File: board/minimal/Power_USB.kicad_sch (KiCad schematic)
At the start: 11 parts, among them J2 USB_C_Receptacle_USB2.0_16P, U4 STUSB4500QTR

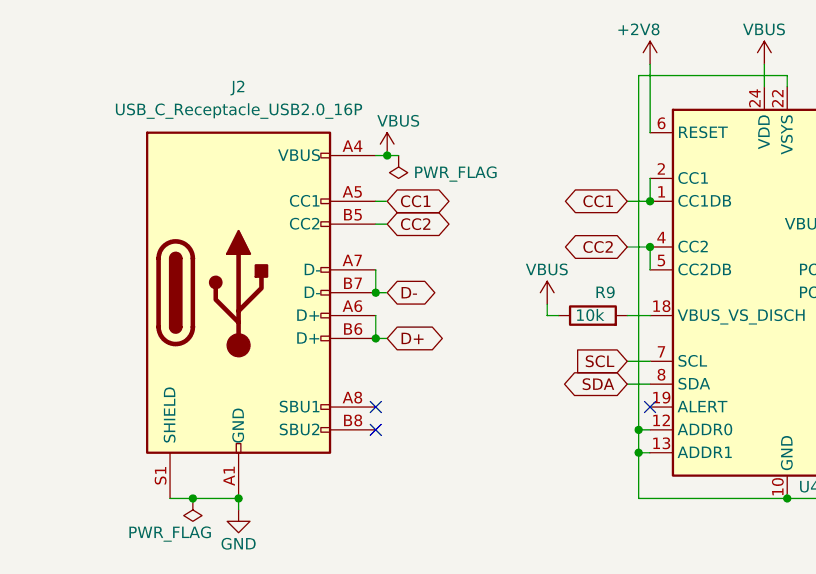
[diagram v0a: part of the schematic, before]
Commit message: change core to rp2350b and some pin out
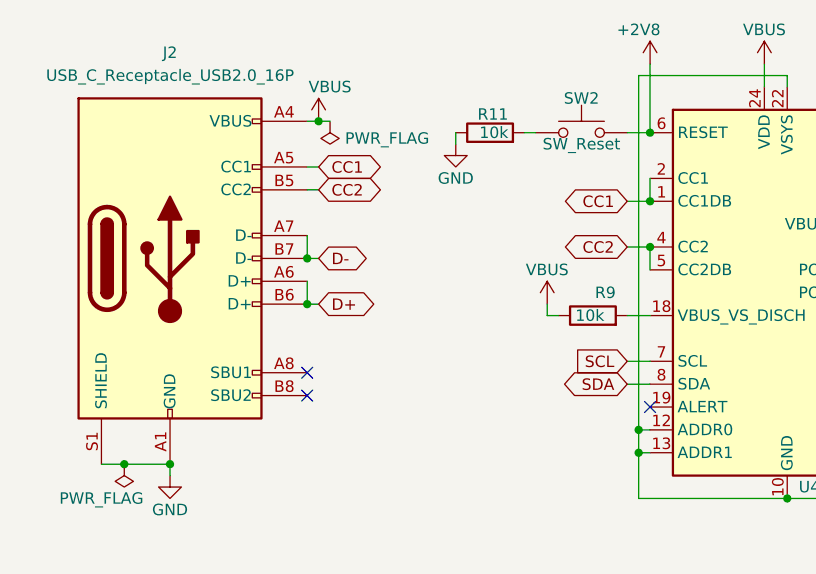
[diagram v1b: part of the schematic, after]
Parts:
- added R11: 10k, Resistor_SMD:R_0603_1608Metric, symbol Device:R
- added SW2: SW_Reset, SW_SKRPACE010:SW_SKRPACE010, symbol Switch:SW_Push
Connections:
- net +2V8: now also SW2.2
- net GND: now also R11.1
- new net: R11.2, SW2.1
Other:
- moved on the sheet: J2

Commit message: add some connectors
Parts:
- added C30: 0.1u, Capacitor_SMD:C_0201_0603Metric, symbol Device:C
- added J17: Jack-DC, symbol Connector:Jack-DC
- added JP4: Jumper_Power, symbol Jumper:Jumper_3_Open
- added Q2: DMP6050SSD, Package_SO:SOIC-8_3.9x4.9mm_P1.27mm, symbol Transistor_FET:DMP6050SSD
- added R20: 100k, Resistor_SMD:R_0603_1608Metric, symbol Device:R
- added R21: 1k, Resistor_SMD:R_0603_1608Metric, symbol Device:R
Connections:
- net GND: now also J17.2
- net PW_EN: now also Q2.2 (G1), Q2.4 (G2), R20.2, R21.1
- net VBUS: now also JP4.2 (C); no longer J2.A4 (VBUS), J2.A9 (VBUS), J2.B4 (VBUS), J2.B9 (VBUS), R10.2
- new net: Q2.1 (S1), Q2.3 (S2), R20.1
- new net: Q2.7 (D1), Q2.8 (D1), R10.2
- new net: C30.2, R21.2
- new net VBUS_{JACK}: J17.1
- new net VBUS_{USB}: C30.1, J2.A4 (VBUS), J2.A9 (VBUS), J2.B4 (VBUS), J2.B9 (VBUS), JP4.1 (A), JP4.3 (B), Q2.5 (D2), Q2.6 (D2)

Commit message: set footprint
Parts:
- J2: renamed from J17; footprint (none) -> Connector_BarrelJack:BarrelJack_Horizontal
- JP1: renamed from JP4; footprint (none) -> Connector_PinHeader_2.54mm:PinHeader_1x03_P2.54mm_Vertical
- renumbered C19 to C23, C20 to C24, C30 to C25, J2 to J3, Q2 to Q1, R11 to R12, R9 to R13, R6 to R14, R7 to R15, R8 to R16, R10 to R17, R20 to R18, R21 to R19
